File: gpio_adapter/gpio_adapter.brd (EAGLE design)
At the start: 28.6 x 21.6 mm, 6 parts

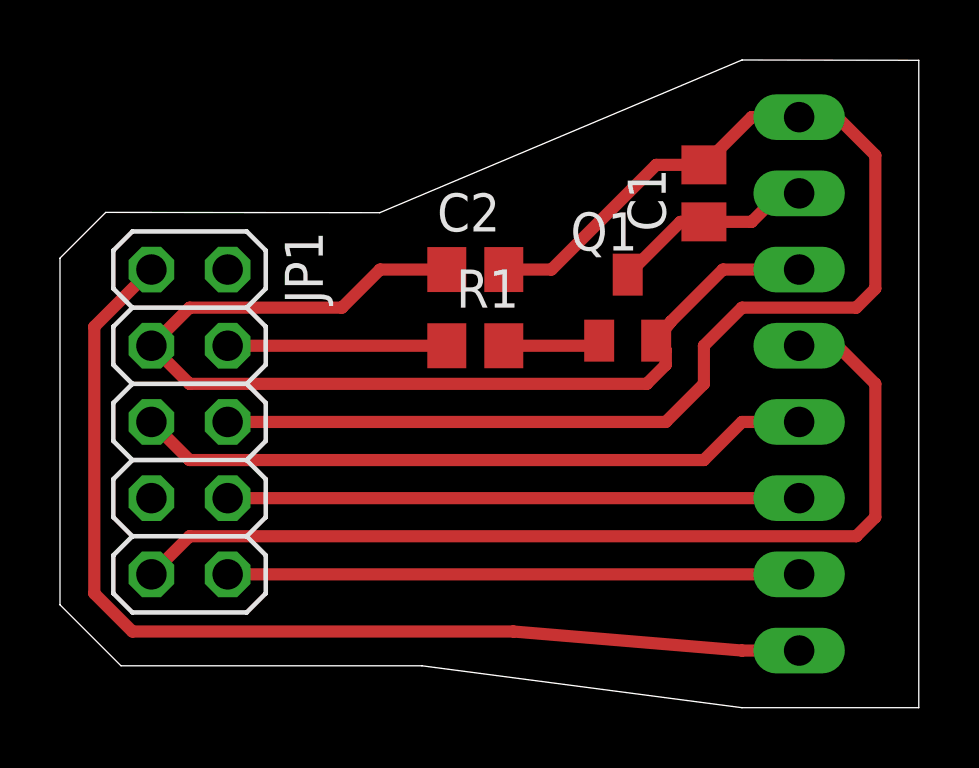
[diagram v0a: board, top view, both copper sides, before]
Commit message: modified board: size optimization
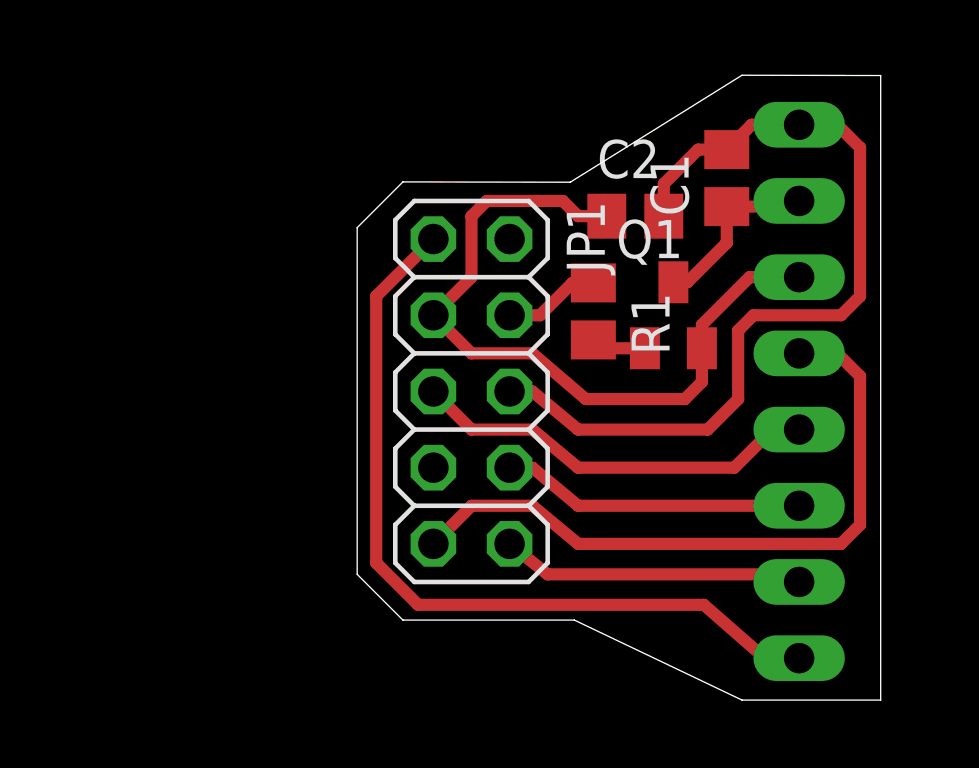
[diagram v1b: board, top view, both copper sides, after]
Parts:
- moved JP1 9.45 mm to (14.5, 11.2)
- moved C2 5.62 mm to (19.9, 17.0)
- moved R1 4.10 mm to (18.5, 13.8), turned to 270 degrees
- moved Q1 1.55 mm to (21.2, 13.7)
- moved C1 0.92 mm to (23.0, 18.3)
- moved JP2 0.25 mm to (29.2, 11.2)
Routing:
- net GND: track 43.6 -> 29.0 mm
- net +3V3: track 35.6 -> 24.8 mm
- net LCD_CLK: track 32.4 -> 22.8 mm
- net LCD_MOSI: track 22.6 -> 13.7 mm
- net LCD_DC: track 19.0 -> 10.1 mm
- net LCD_CS: track 19.0 -> 10.1 mm
- net LCD_RST: track 35.6 -> 26.9 mm
- net BACKLIGHT_SIGNAL: track 7.30 -> 3.24 mm
- net N$2: track 3.25 -> 1.83 mm
- net V_BACKLIGHT: track 6.84 -> 5.98 mm
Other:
- board size 28.6 x 21.6 mm -> 17.4 x 20.8 mm
